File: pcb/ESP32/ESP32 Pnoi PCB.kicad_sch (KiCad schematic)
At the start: 6 parts

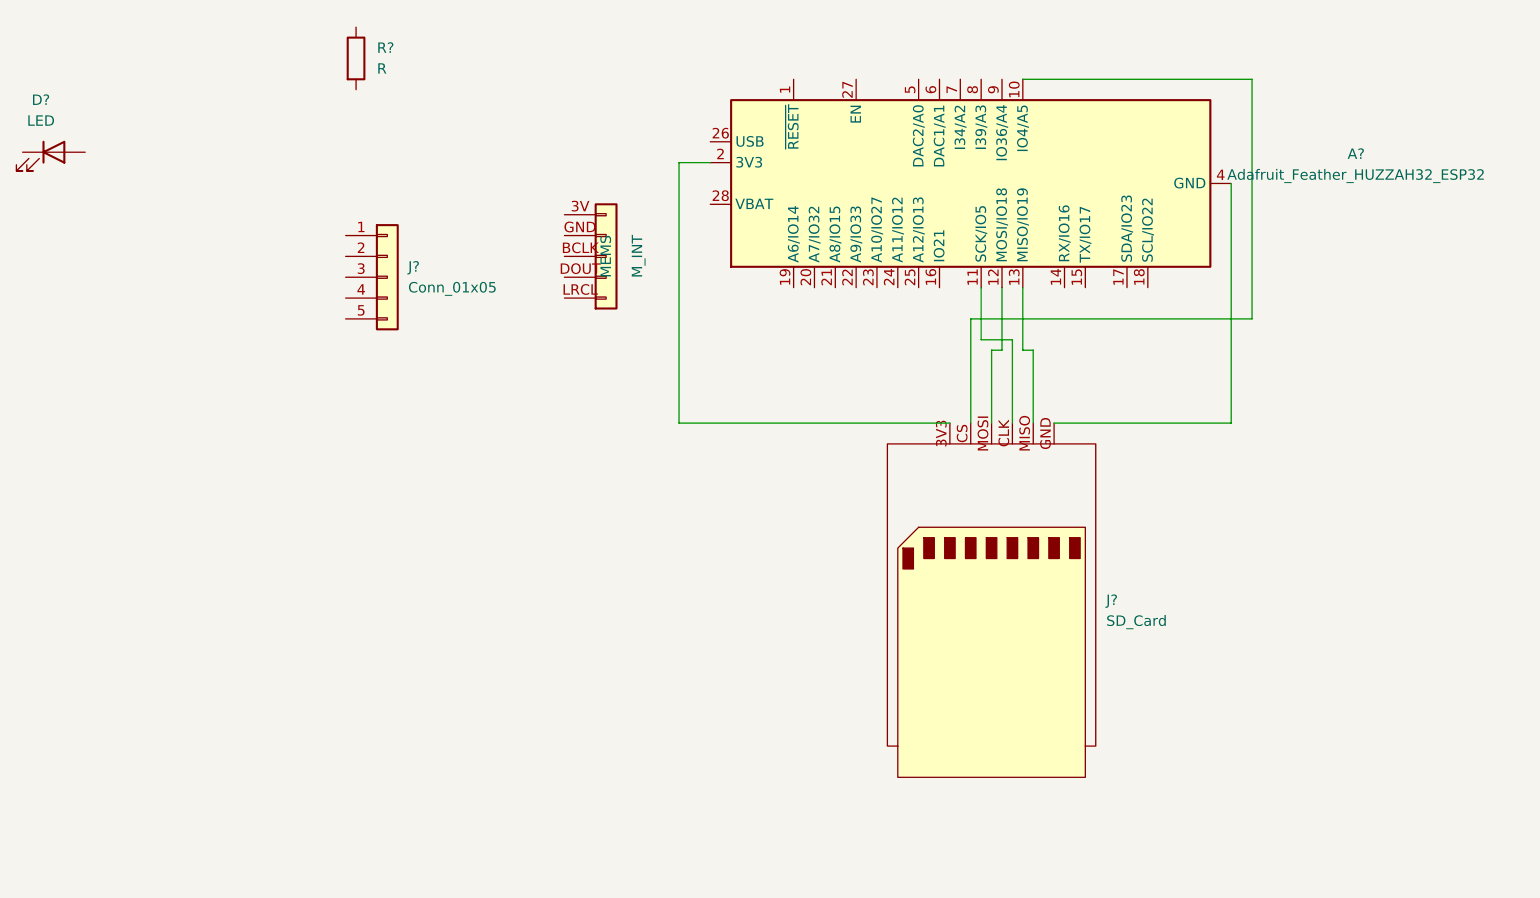
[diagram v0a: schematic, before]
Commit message: Complete ESP32 PCB
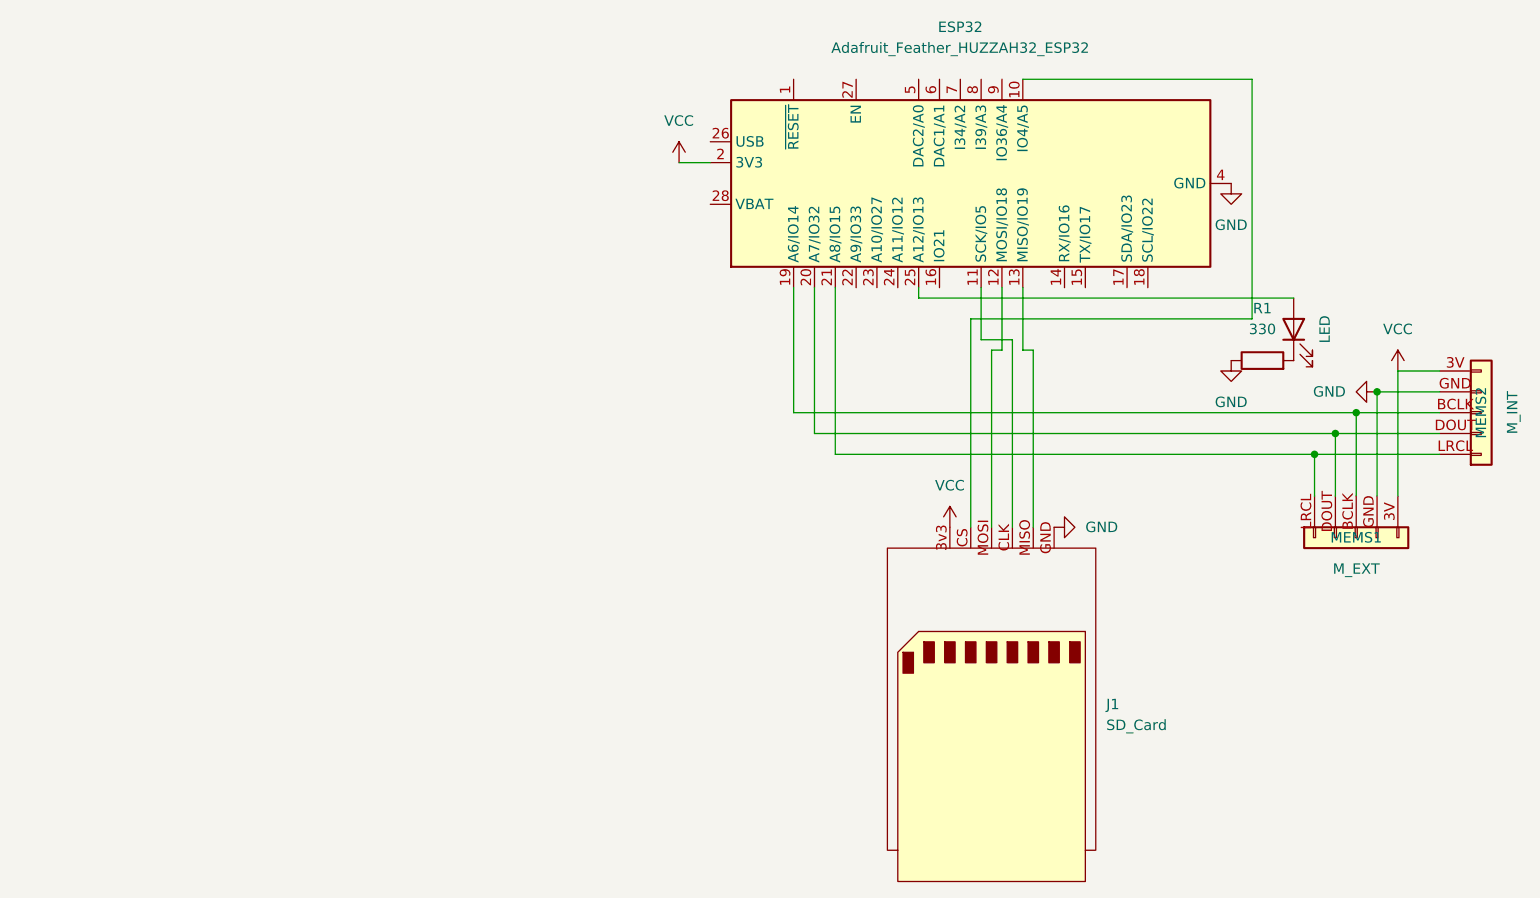
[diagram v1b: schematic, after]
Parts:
- removed J?: Conn_01x05, symbol Connector_Generic:Conn_01x05
- added MEMS1: M_EXT, Pnoi Footprints:5-Pin MEMS Connector, symbol Connector_Generic:Conn_01x05
- D1: renamed from D?; footprint (none) -> LED_THT:LED_D3.0mm
- ESP32: renamed from A?; footprint Module:Adafruit_Feather -> Module:Adafruit_Feather_WithMountingHoles
- J1: renamed from J?; footprint (none) -> Pnoi Footprints:6-Pin SD Card Connector
- MEMS2: renamed from MEMS; footprint (none) -> Pnoi Footprints:5-Pin MEMS Connector
- R1: renamed from R?; value R -> 330; footprint (none) -> Resistor_THT:R_Axial_DIN0204_L3.6mm_D1.6mm_P5.08mm_Horizontal
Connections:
- net at ESP32.19 (A6/IO14): now also MEMS2.BCLK, MEMS1.BCLK
- net VCC: now reaches ESP32.2 (3V3)
- net VCC: now also J1.3v3, MEMS2.3V, MEMS1.3V; no longer J1.3V3
- net at ESP32.20 (A7/IO32): now also MEMS2.DOUT, MEMS1.DOUT
- net at ESP32.21 (A8/IO15): now also MEMS2.LRCL, MEMS1.LRCL
- net at ESP32.25 (A12/IO13): now also D1.2 (A)
- net GND: now reaches ESP32.4 (GND), J1.GND
- net GND: now also MEMS2.GND, R1.1, MEMS1.GND
- net at R1.2: now also D1.1 (K)
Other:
- moved on the sheet: J1, MEMS2, R1
